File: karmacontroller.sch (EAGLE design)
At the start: 19 parts

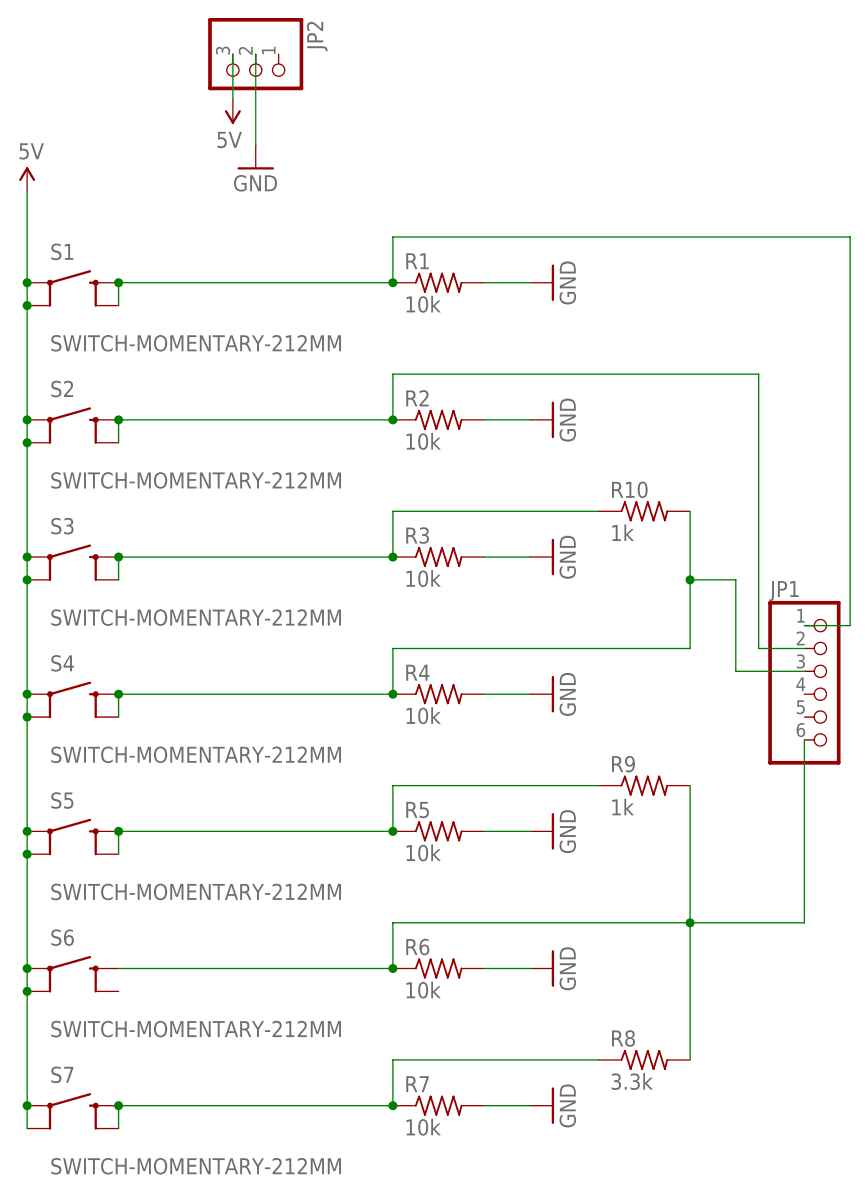
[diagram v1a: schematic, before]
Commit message: Upgraded board and software
- I changed all the resistors to the Sparkfun AXIAL-0.3 and rerouted
everything.
- I changed the mask limit to 25mil.
- I moved the "Karma Controller" text over to the left.
- I hid the tOrigins layer. These are the crosshairs.
- I updated the date to 6/25/2013
- I updated the software to use the analog values for the new 4.7K
resistor
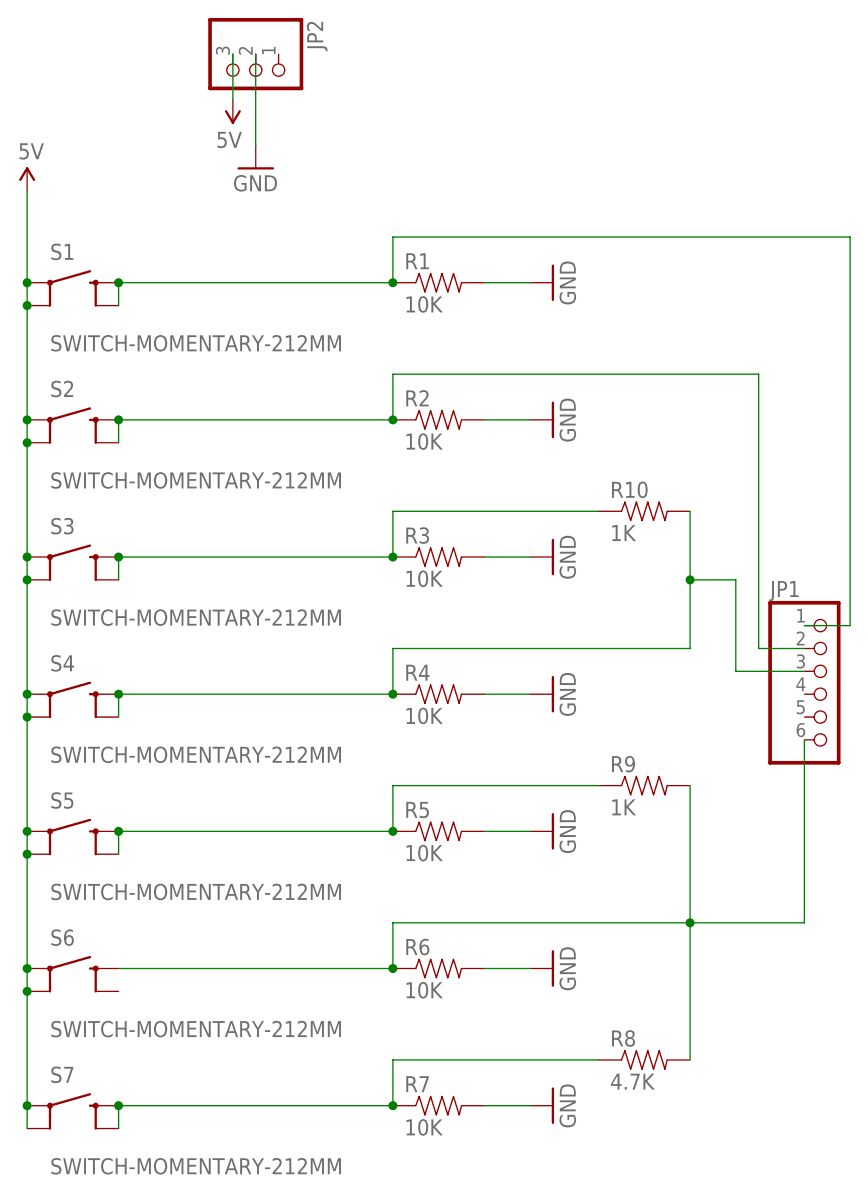
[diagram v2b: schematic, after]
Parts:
- R1, R2, R3, R4, R5, R6, R7: value 10k -> 10K; device rcl:R-US_0207/10 -> SparkFun-Resistors:RESISTORAXIAL-0.3
- R10, R9: value 1k -> 1K; device rcl:R-US_0207/10 -> SparkFun-Resistors:RESISTORAXIAL-0.3
- R8: value 3.3k -> 4.7K; device rcl:R-US_0207/10 -> SparkFun-Resistors:RESISTORAXIAL-0.3
